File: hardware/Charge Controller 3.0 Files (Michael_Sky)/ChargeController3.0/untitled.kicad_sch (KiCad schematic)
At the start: 2 parts, among them J1 Conn_02x26_Odd_Even, J12 Conn_02x26_Odd_Even

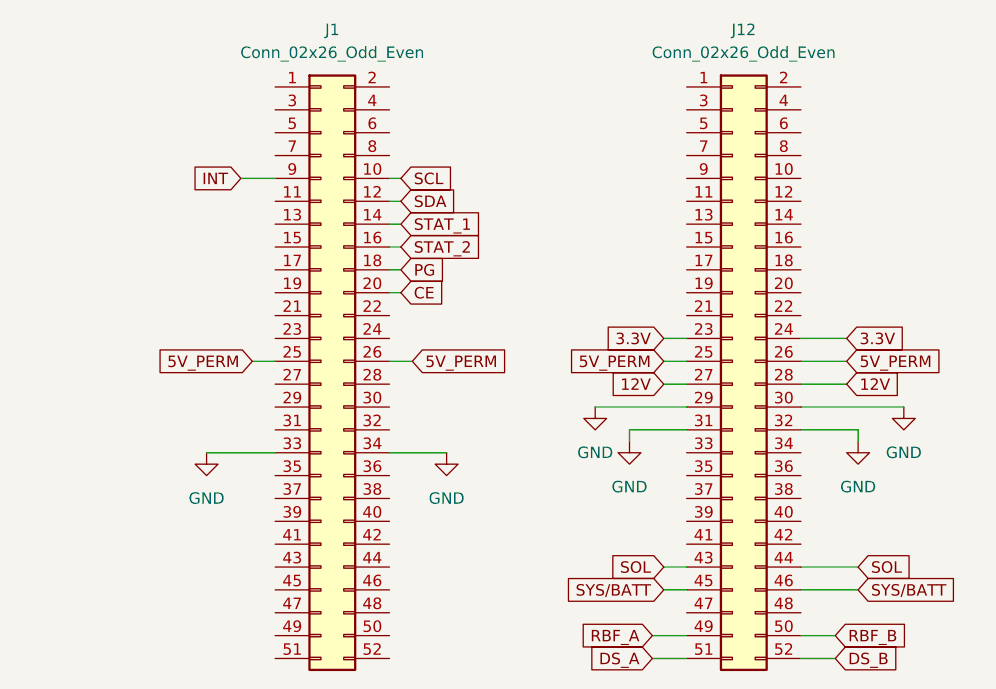
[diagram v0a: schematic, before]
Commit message: Added template, reassigned pins
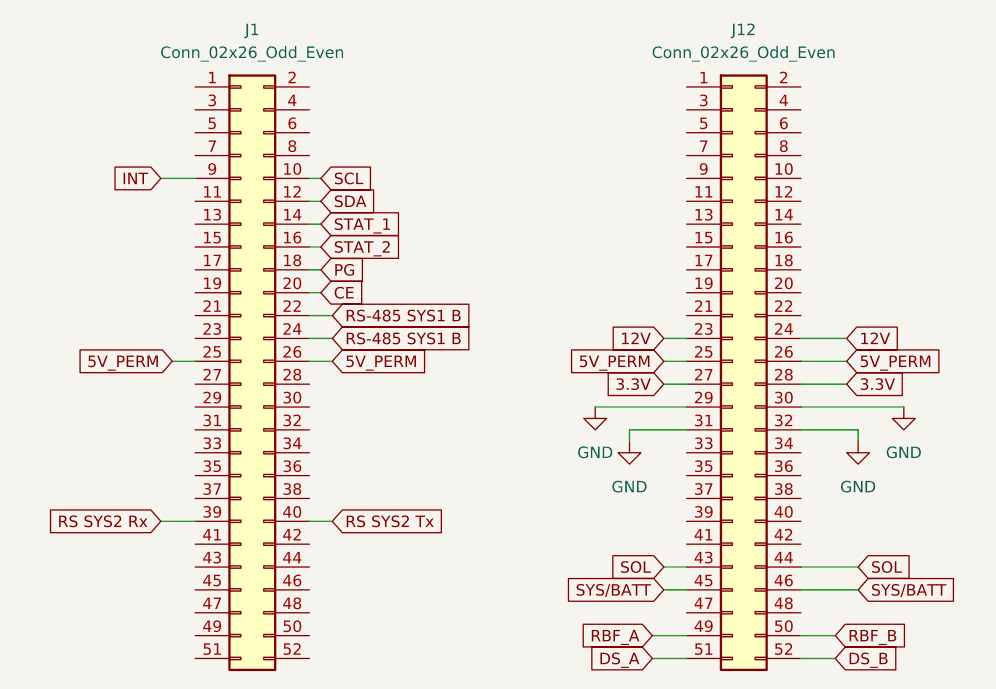
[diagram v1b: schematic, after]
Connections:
- net 12V: now also J12.23 (Pin_23), J12.24 (Pin_24); no longer J12.27 (Pin_27), J12.28 (Pin_28)
- net 3.3V: now also J12.27 (Pin_27), J12.28 (Pin_28); no longer J12.23 (Pin_23), J12.24 (Pin_24)
- net GND: no longer J1.33 (Pin_33), J1.34 (Pin_34)
- net RS-485 SYS1 B: now reaches J1.22 (Pin_22)
- net RS-485 SYS1 B: now also J1.24 (Pin_24)
- net RS SYS2 Rx: now reaches J1.39 (Pin_39)
- net RS SYS2 Tx: now reaches J1.40 (Pin_40)
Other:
- moved on the sheet: J1
